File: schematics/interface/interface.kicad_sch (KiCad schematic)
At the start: 12 parts, among them J3 Conn_02x25_Counter_Clockwise, U1 74LS00, U2 74LS02, U4 74LS245, U5 74LS193, U6 74LS193, U7 74LS193, U8 74LS193

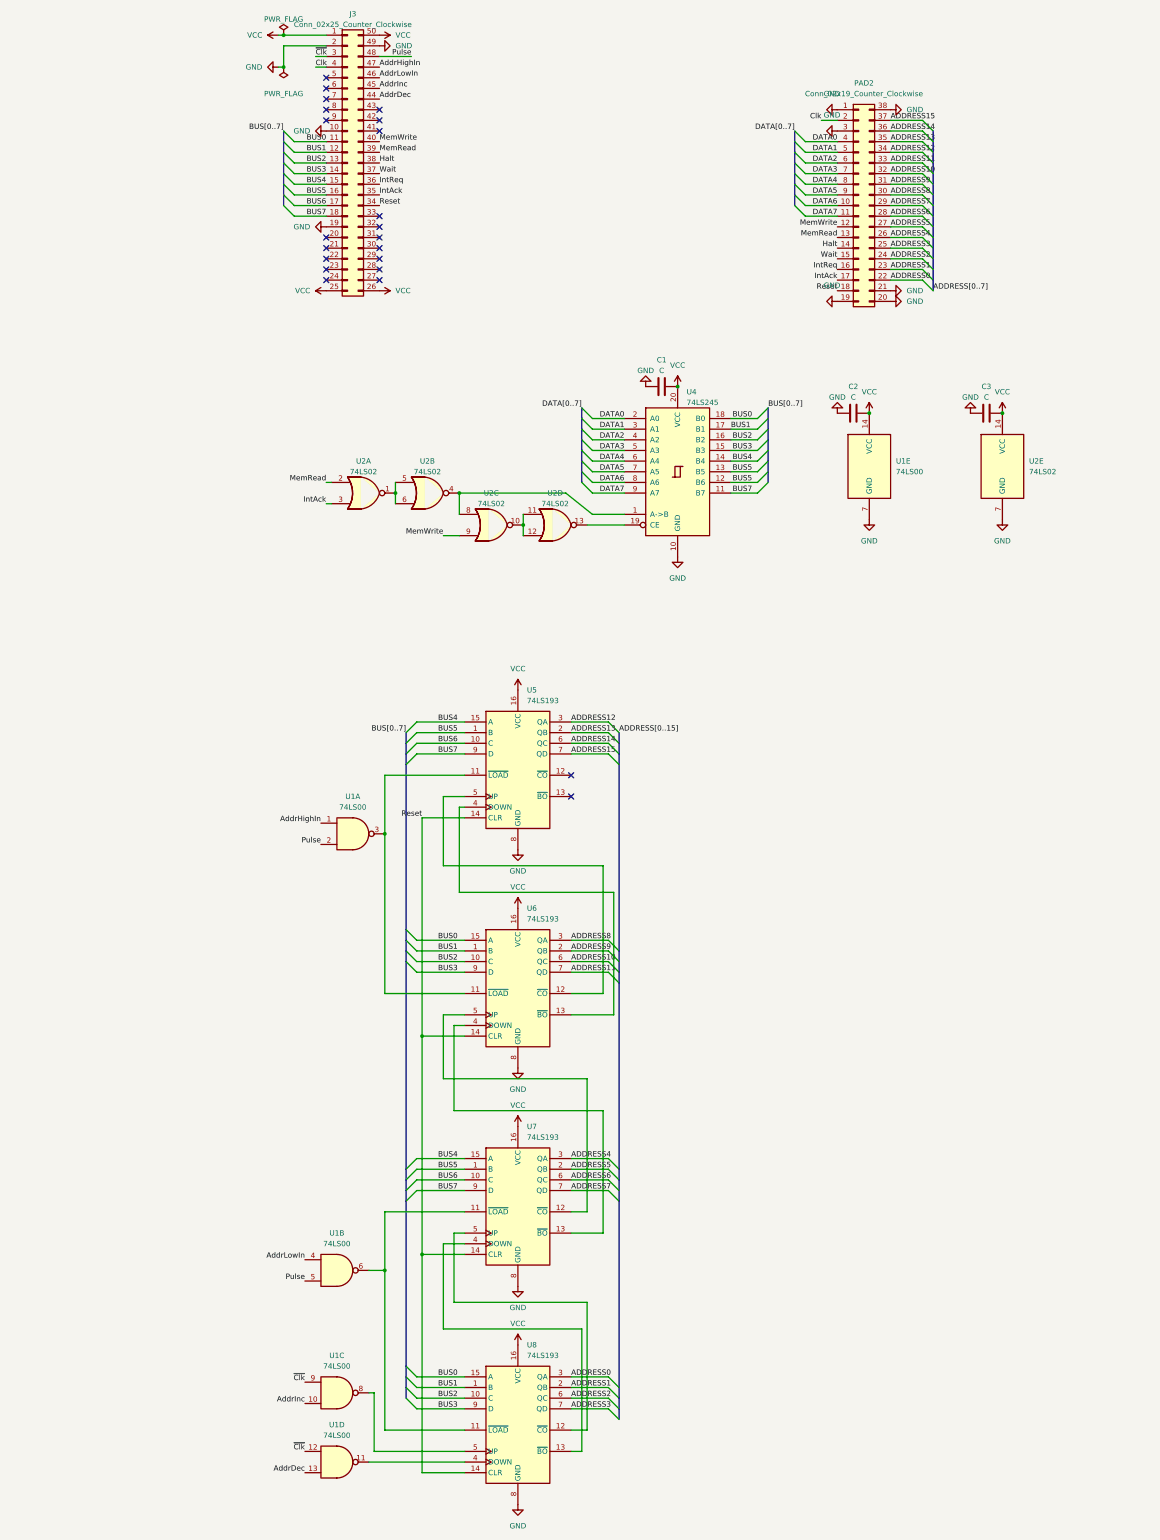
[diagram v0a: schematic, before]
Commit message: structure(kicad): redefined the structure of the repository
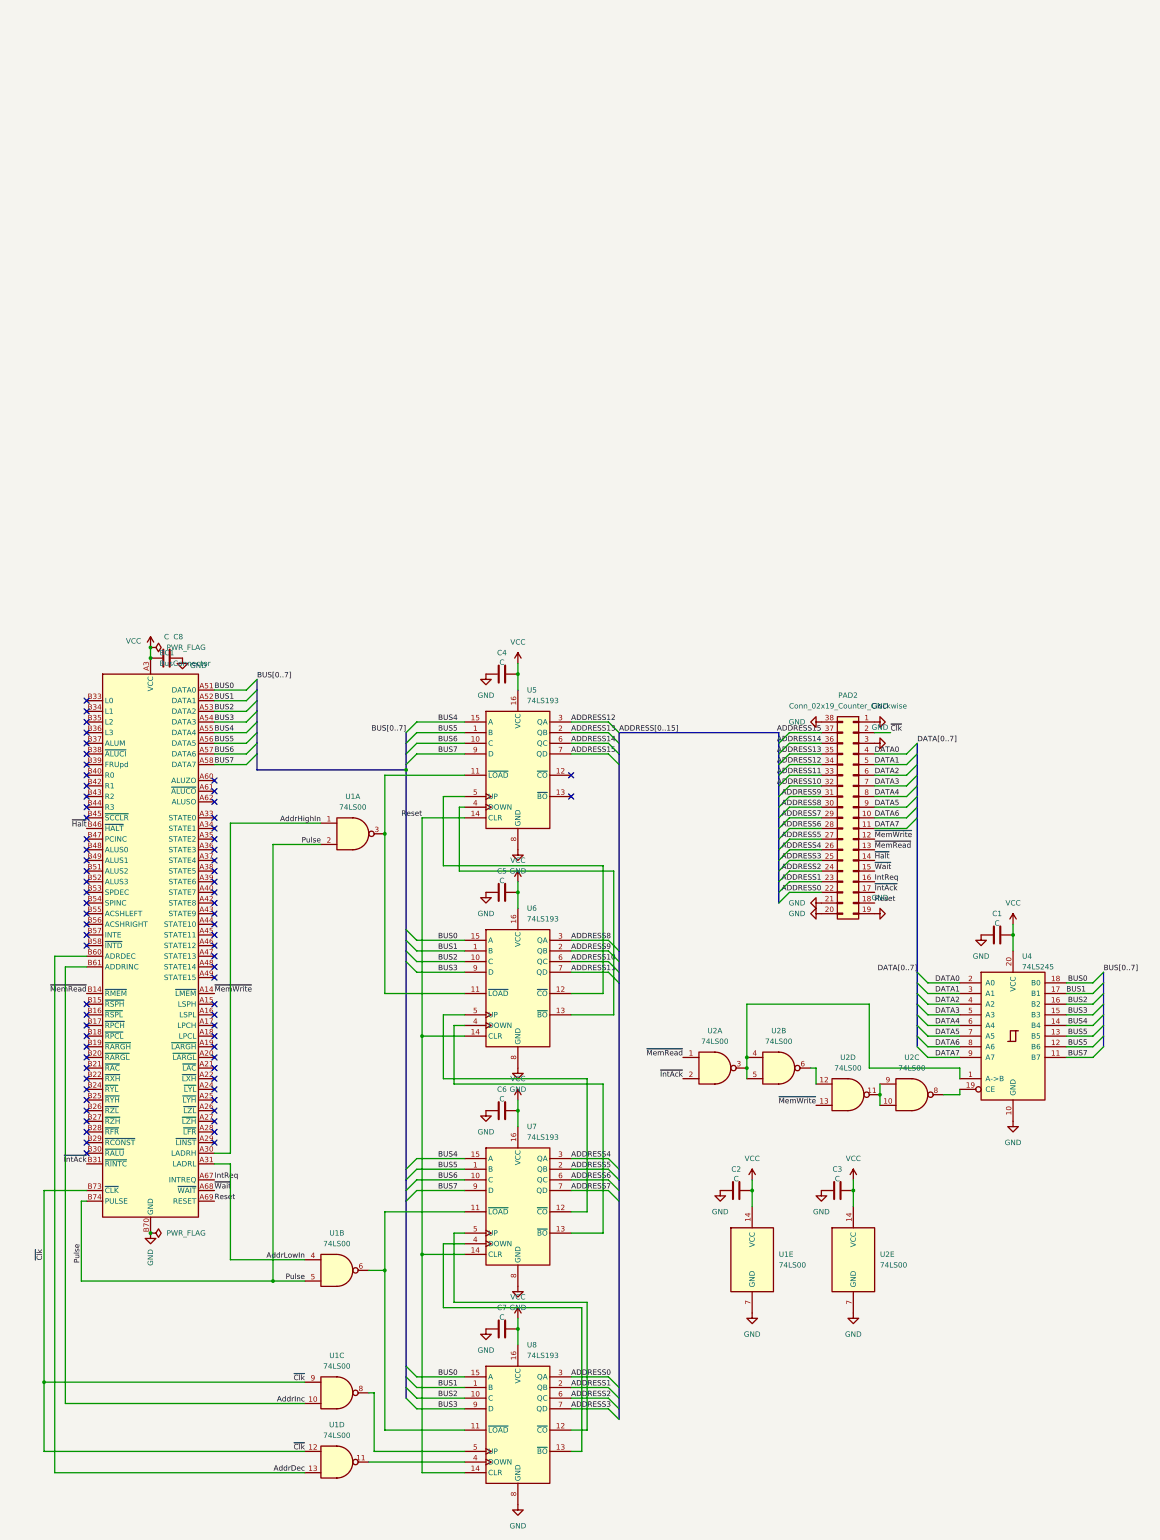
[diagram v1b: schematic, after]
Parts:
- removed J3: Conn_02x25_Counter_Clockwise, Connector_PinSocket_2.54mm:PinSocket_2x25_P2.54mm_Horizontal, symbol Connector_Generic:Conn_02x25_Counter_Clockwise
- removed U2: 74LS02, Package_DIP:DIP-14_W7.62mm_Socket_LongPads, symbol 74xx:74LS02
- added BC1: BusConnector, Connector_PCBEdge:BUS_PCIexpress_x16, symbol cpu816symbols:BusConnector
- added C4, C5, C6, C7: C, Capacitor_THT:C_Disc_D5.0mm_W2.5mm_P5.00mm, symbol Device:C
- added C8: C, Capacitor_THT:C_Radial_D6.3mm_H5.0mm_P2.50mm, symbol Device:C
- added U2: 74LS00, Package_DIP:DIP-14_W7.62mm_Socket_LongPads, symbol 74xx:74LS00
- C1, C2, C3: footprint (none) -> Capacitor_THT:C_Disc_D5.0mm_W2.5mm_P5.00mm
- PAD2: footprint Connector_PinSocket_2.54mm:PinSocket_2x19_P2.54mm_Horizontal -> Connector_PinSocket_2.54mm:PinSocket_2x19_P2.54mm_Vertical
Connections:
- net Clk is gone; now on net ~{Clk}: PAD2.2 (Pin_2)
- net AddrDec: now also BC1.B60 (ADRDEC)
- net AddrHighIn: now also BC1.A30 (LADRH)
- net AddrInc: now also BC1.B61 (ADDRINC)
- net AddrLowIn: now also BC1.A31 (LADRL)
- net BUS0: now also BC1.A51 (DATA0)
- net BUS1: now also BC1.A52 (DATA1)
- net BUS2: now also BC1.A53 (DATA2)
- net BUS3: now also BC1.A54 (DATA3)
- net BUS4: now also BC1.A55 (DATA4)
- net BUS5: now also BC1.A56 (DATA5)
- net BUS6: now also BC1.A57 (DATA6)
- net BUS7: now also BC1.A58 (DATA7)
- net GND: now also C1.2, C2.2, C3.2, BC1.A12 (GND), BC1.A13 (GND), BC1.A23 (GND), BC1.A32 (GND), BC1.A41 (GND), BC1.A50 (GND), BC1.A59 (GND), BC1.A63 (GND), BC1.A64 (GND), BC1.A65 (GND), BC1.A66 (GND), BC1.A70 (GND), BC1.A71 (GND), BC1.A72 (GND), BC1.A73 (GND), BC1.A74 (GND), BC1.A75 (GND), BC1.A76 (GND), BC1.B12 (GND), BC1.B13 (GND), BC1.B23 (GND), BC1.B32 (GND), BC1.B41 (GND), BC1.B50 (GND), BC1.B59 (GND), BC1.B62 (GND), BC1.B63 (GND), BC1.B64 (GND), BC1.B65 (GND), BC1.B66 (GND), BC1.B67 (GND), BC1.B68 (GND), BC1.B69 (GND), BC1.B70 (GND), BC1.B71 (GND), BC1.B72 (GND), BC1.B75 (GND), BC1.B76 (GND), C4.2, C5.2, C6.2, C7.2, C8.2, U2.7 (GND); no longer C1.1, C2.1, C3.1
- net IntReq: now also BC1.A67 (INTREQ)
- net Pulse: now also BC1.B74 (PULSE)
- net Reset: now also BC1.A69 (RESET)
- net VCC: now also C1.1, C2.1, C3.1, BC1.A1 (VCC), BC1.A2 (VCC), BC1.A3 (VCC), BC1.A4 (VCC), BC1.A5 (VCC), BC1.B1 (VCC), BC1.B2 (VCC), BC1.B3 (VCC), BC1.B4 (VCC), BC1.B5 (VCC), C4.1, C5.1, C6.1, C7.1, C8.1, U2.14 (VCC); no longer C1.2, C2.2, C3.2
- net ~{Clk}: now also BC1.B73 (~{CLK})
- net at U4.1 (A->B): now also U2.3, U2.4, U2.5
- net at U4.19 (CE): now also U2.8
- net Halt renamed ~{Halt}
- net ~{Halt}: now also BC1.B46 (~{HALT})
- net IntAck renamed ~{IntAck}
- net ~{IntAck}: now also BC1.B31 (~{RINTC}), U2.2
- net MemRead renamed ~{MemRead}
- net ~{MemRead}: now also BC1.B14 (~{RMEM}), U2.1
- net MemWrite renamed ~{MemWrite}
- net ~{MemWrite}: now also BC1.A14 (~{LMEM}), U2.13
- net Wait renamed ~{Wait}
- net ~{Wait}: now also BC1.A68 (~{WAIT})
- new net: U2.10, U2.11, U2.9
- new net: U2.12, U2.6
- no-connect marks 22 -> 73
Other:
- moved on the sheet: PAD2, U1E, U4

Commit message: Add test points
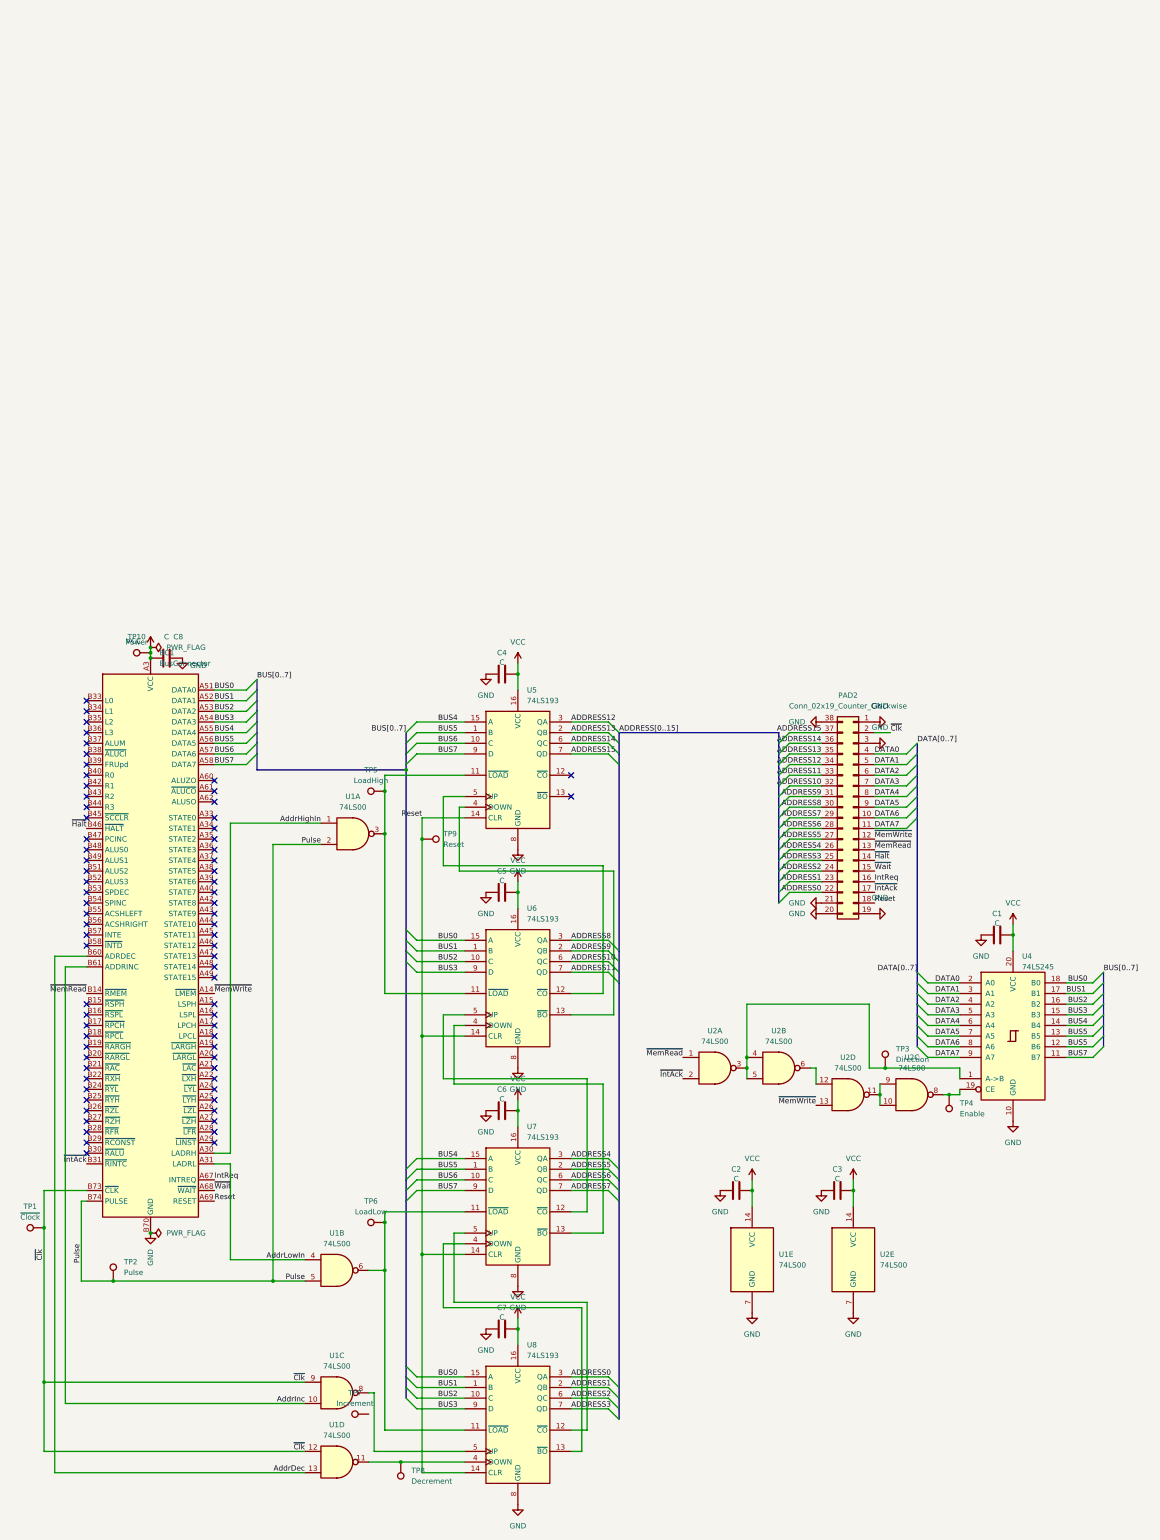
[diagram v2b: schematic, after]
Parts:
- added TP1: ~{Clock}, Connector_Pin:Pin_D1.0mm_L10.0mm, symbol Connector:TestPoint
- added TP10: Power, Connector_Pin:Pin_D1.0mm_L10.0mm, symbol Connector:TestPoint
- added TP2: Pulse, Connector_Pin:Pin_D1.0mm_L10.0mm, symbol Connector:TestPoint
- added TP3: Direction, Connector_Pin:Pin_D1.0mm_L10.0mm, symbol Connector:TestPoint
- added TP4: Enable, Connector_Pin:Pin_D1.0mm_L10.0mm, symbol Connector:TestPoint
- added TP5: LoadHigh, Connector_Pin:Pin_D1.0mm_L10.0mm, symbol Connector:TestPoint
- added TP6: LoadLow, Connector_Pin:Pin_D1.0mm_L10.0mm, symbol Connector:TestPoint
- added TP7: Increment, Connector_Pin:Pin_D1.0mm_L10.0mm, symbol Connector:TestPoint
- added TP8: Decrement, Connector_Pin:Pin_D1.0mm_L10.0mm, symbol Connector:TestPoint
- added TP9: Reset, Connector_Pin:Pin_D1.0mm_L10.0mm, symbol Connector:TestPoint
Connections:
- net Pulse: now also TP2.1
- net Reset: now also TP9.1
- net VCC: now also TP10.1
- net ~{Clk}: now also TP1.1
- net at U2.3, U2.4, U2.5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: now also TP3.1
- net at U1.3, U5.11 (~{LOAD}), U6.11 (~{LOAD}): now also TP5.1
- net at U2.8, U4.19 (CE): now also TP4.1
- net at U1.11, U8.4 (DOWN): now also TP8.1
- net at U1.6, U7.11 (~{LOAD}), U8.11 (~{LOAD}): now also TP6.1
